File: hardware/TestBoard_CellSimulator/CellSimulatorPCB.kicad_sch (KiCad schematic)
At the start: 14 parts, among them J1 575-4, J11 Conn_01x07, J2 575-4

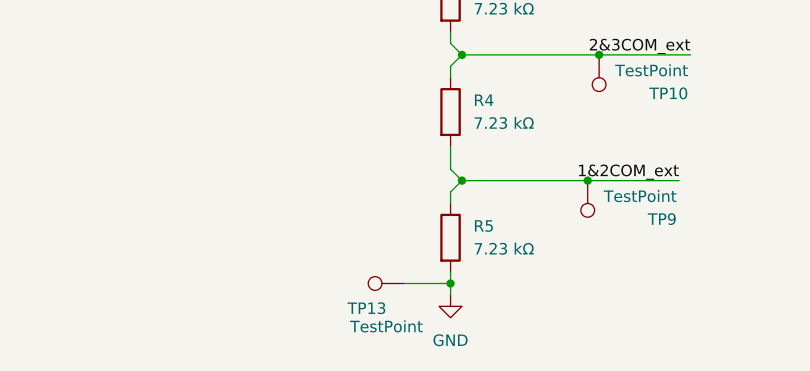
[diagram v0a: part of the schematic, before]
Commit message: bom for cell sim and thermistor
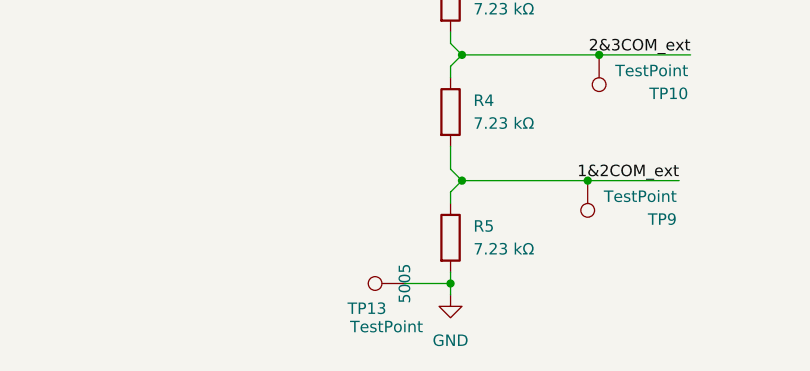
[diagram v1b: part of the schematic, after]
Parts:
- J11: P/N (none) -> 1053131107
- TP10, TP11, TP12, TP13, TP14, TP9: P/N (none) -> 5005
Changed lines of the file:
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@@
+			)
+		)
+		(property "P/N" "5005"
+			(at 114.3 142.24 0)
+			(effects
+				(font
+					(size 1.27 1.27)
+				)
 			)
 		)
@@
 			)
 		)
+		(property "P/N" "1053131107"
+			(at 165.1 68.58 0)
+			(effects
+				(font
+					(size 1.27 1.27)
+				)
+				(hide yes)
+			)
+		)
 		(pin "6"
 		)
@@
 			)
 		)
+		(property "P/N" "5005"
+			(at 134.62 130.81 0)
+			(effects
+				(font
+					(size 1.27 1.27)
+				)
+				(hide yes)
+			)
+		)
 		(pin "1"
 		)
@@
 			)
 		)
+		(property "P/N" "5005"
+			(at 113.03 80.01 0)
+			(effects
+				(font
+					(size 1.27 1.27)
+				)
+				(hide yes)
+			)
+		)
 		(pin "1"
 		)
@@
 		)
 		(property "Description" "test point"
+			(at 135.89 91.44 0)
+			(effects
+				(font
+					(size 1.27 1.27)
+				)
+				(hide yes)
+			)
+		)
+		(property "P/N" "5005"
 			(at 135.89 91.44 0)
 			(effects
@@
 			)
 		)
+		(property "P/N" "5005"
+			(at 135.89 116.84 0)
+			(effects
+				(font
+					(size 1.27 1.27)
+				)
+				(hide yes)
+			)
+		)
 		(pin "1"
 		)
@@
 			(at 135.89 104.14 0)
 			(effects
+				(font
+					(size 1.27 1.27)
+				)
+				(hide yes)
+			)
+		)
+		(property "P/N" "5005"
+			(at 135.89 104.14 0)
+			(effects
